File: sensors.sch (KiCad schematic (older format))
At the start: 21 parts, among them U2 LIS2DH12TR, U3 L3GD20HTR, U4 MP6515GF-Z, U5 MP6515GF-Z, U6 MP6515GF-Z

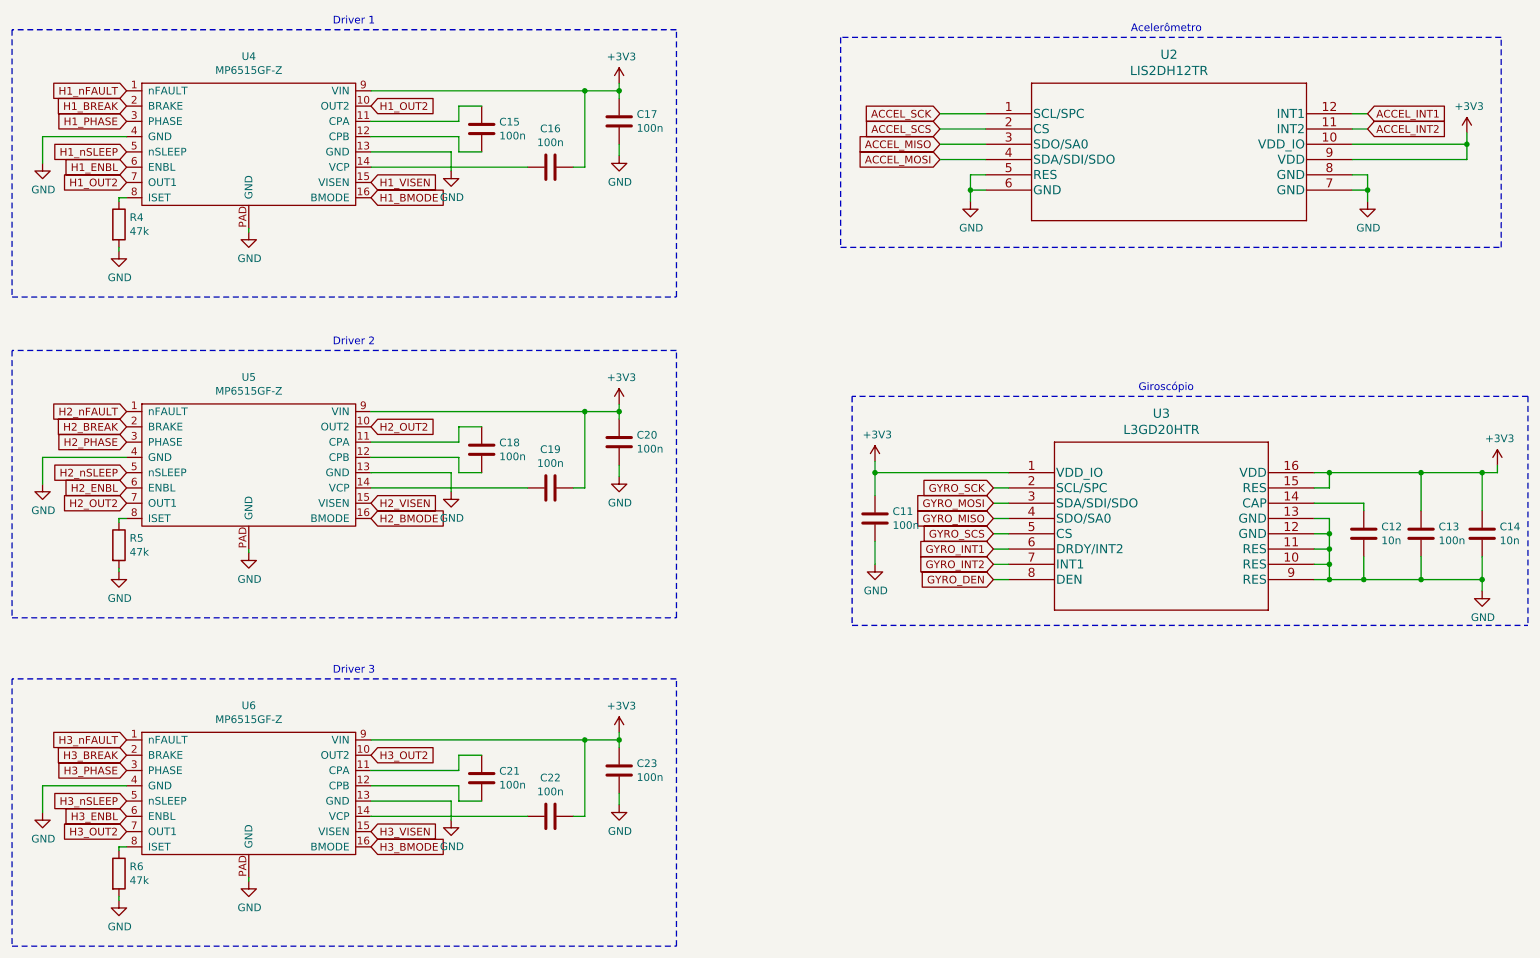
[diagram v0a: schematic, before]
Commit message: wiring sensors
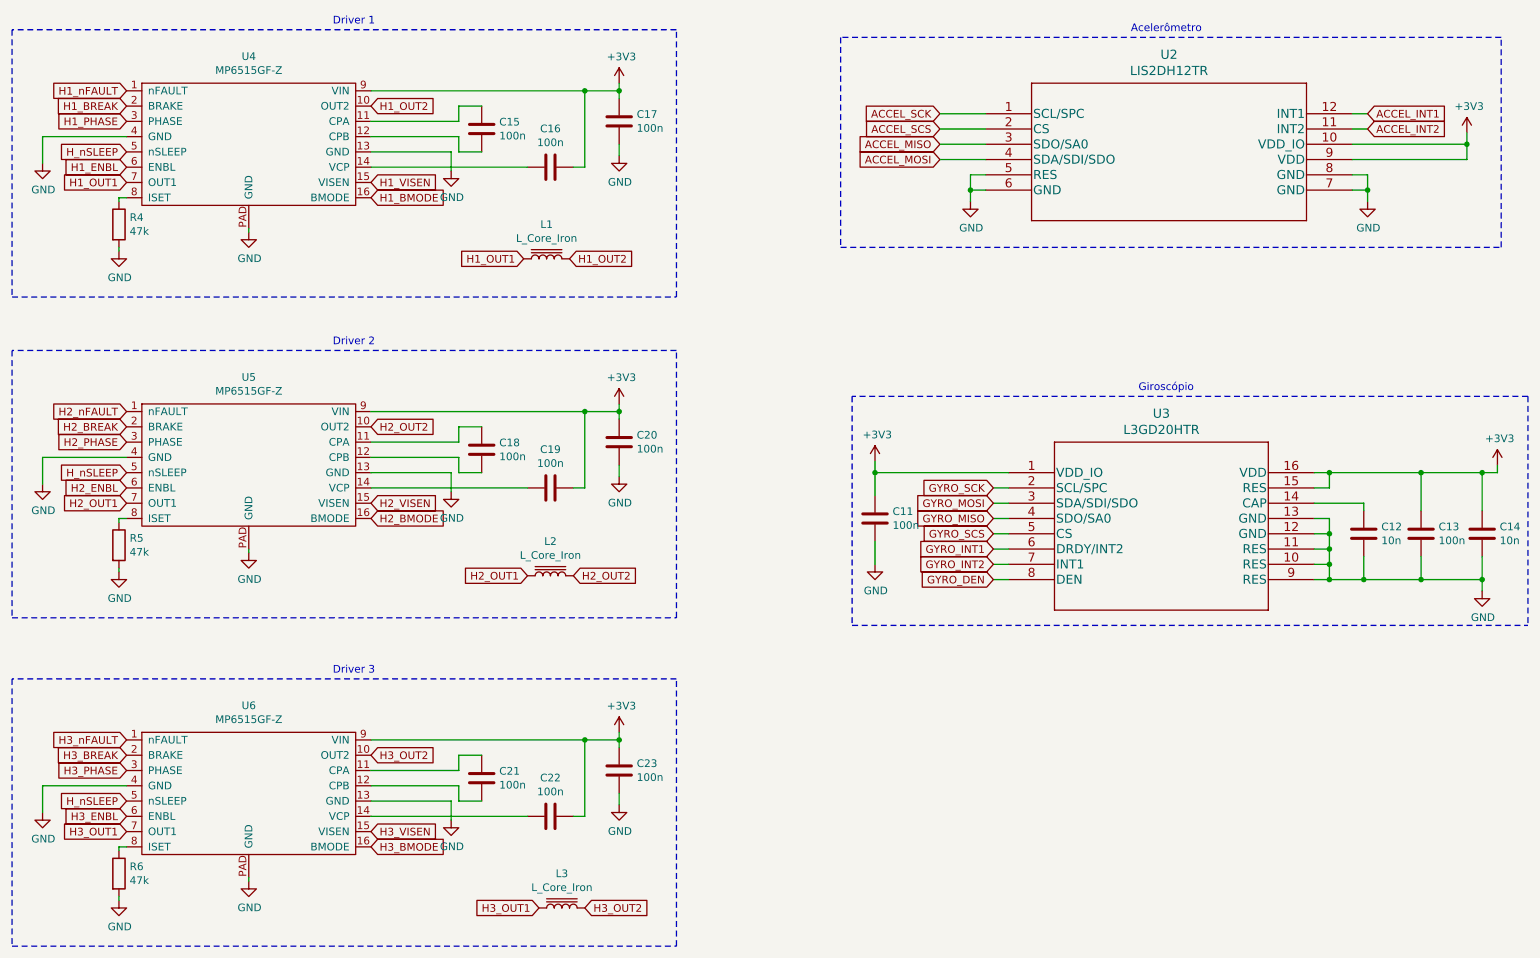
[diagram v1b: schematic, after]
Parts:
- added L1, L2, L3: L_Core_Iron, symbol Device:L_Core_Iron
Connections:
- net H2_nSLEEP is gone; now on net H_nSLEEP: U5.5 (nSLEEP)
- net H3_nSLEEP is gone; now on net H_nSLEEP: U6.5 (nSLEEP)
- net H1_OUT2: now also L1.2; no longer U4.7 (OUT1)
- net H2_OUT2: now also L2.2; no longer U5.7 (OUT1)
- net H3_OUT2: now also L3.2; no longer U6.7 (OUT1)
- net H1_nSLEEP renamed H_nSLEEP
- new net H1_OUT1: L1.1, U4.7 (OUT1)
- new net H2_OUT1: L2.1, U5.7 (OUT1)
- new net H3_OUT1: L3.1, U6.7 (OUT1)
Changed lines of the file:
@@
 H1_BREAK
 Text GLabel 1500 2050 0    50   Input ~ 0
-H1_nSLEEP
+H_nSLEEP
 Text GLabel 1500 2150 0    50   Input ~ 0
 H1_ENBL
@@
 H1_OUT2
 Text GLabel 1500 2250 0    50   Input ~ 0
-H1_OUT2
+H1_OUT1
 Wire Notes Line
 	750  3000 5100 3000
@@
 H2_BREAK
 Text GLabel 1500 4150 0    50   Input ~ 0
-H2_nSLEEP
+H_nSLEEP
 Text GLabel 1500 4250 0    50   Input ~ 0
 H2_ENBL
@@
 H2_OUT2
 Text GLabel 1500 4350 0    50   Input ~ 0
-H2_OUT2
+H2_OUT1
 Wire Notes Line
 	750  5100 5100 5100
@@
 H3_BREAK
 Text GLabel 1500 6300 0    50   Input ~ 0
-H3_nSLEEP
+H_nSLEEP
 Text GLabel 1500 6400 0    50   Input ~ 0
 H3_ENBL
@@
 H3_OUT2
 Text GLabel 1500 6500 0    50   Input ~ 0
-H3_OUT2
+H3_OUT1
 Wire Notes Line
 	750  7250 5100 7250
@@
 Text Notes 2850 5475 0    50   ~ 0
 Driver 3
+$Comp
+L Device:L_Core_Iron L1
+U 1 1 61DED93B
+P 4250 2750
+F 0 "L1" V 4475 2750 50  0000 C CNN
+F 1 "L_Core_Iron" V 4384 2750 50  0000 C CNN
+F 2 "" H 4250 2750 50  0001 C CNN
+F 3 "~" H 4250 2750 50  0001 C CNN
+	1    4250 2750
+	0    -1   -1   0
+$EndComp
+Text GLabel 4100 2750 0    50   Input ~ 0
+H1_OUT1
+Text GLabel 4400 2750 2    50   Input ~ 0
+H1_OUT2
+$Comp
+L Device:L_Core_Iron L2
+U 1 1 61DEFF0E
+P 4275 4825
+F 0 "L2" V 4500 4825 50  0000 C CNN
+F 1 "L_Core_Iron" V 4409 4825 50  0000 C CNN
+F 2 "" H 4275 4825 50  0001 C CNN
+F 3 "~" H 4275 4825 50  0001 C CNN
+	1    4275 4825
+	0    -1   -1   0
+$EndComp
+Text GLabel 4125 4825 0    50   Input ~ 0
+H2_OUT1
+Text GLabel 4425 4825 2    50   Input ~ 0
+H2_OUT2
+$Comp
+L Device:L_Core_Iron L3
+U 1 1 61DF580B
+P 4350 7000
+F 0 "L3" V 4575 7000 50  0000 C CNN
+F 1 "L_Core_Iron" V 4484 7000 50  0000 C CNN
+F 2 "" H 4350 7000 50  0001 C CNN
+F 3 "~" H 4350 7000 50  0001 C CNN
+	1    4350 7000
+	0    -1   -1   0
+$EndComp
+Text GLabel 4200 7000 0    50   Input ~ 0
+H3_OUT1
+Text GLabel 4500 7000 2    50   Input ~ 0
+H3_OUT2
 $EndSCHEMATC
